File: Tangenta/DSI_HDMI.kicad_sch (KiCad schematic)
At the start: 40 parts, among them J8 HDMI_19PIN_043, U13 LT8912B

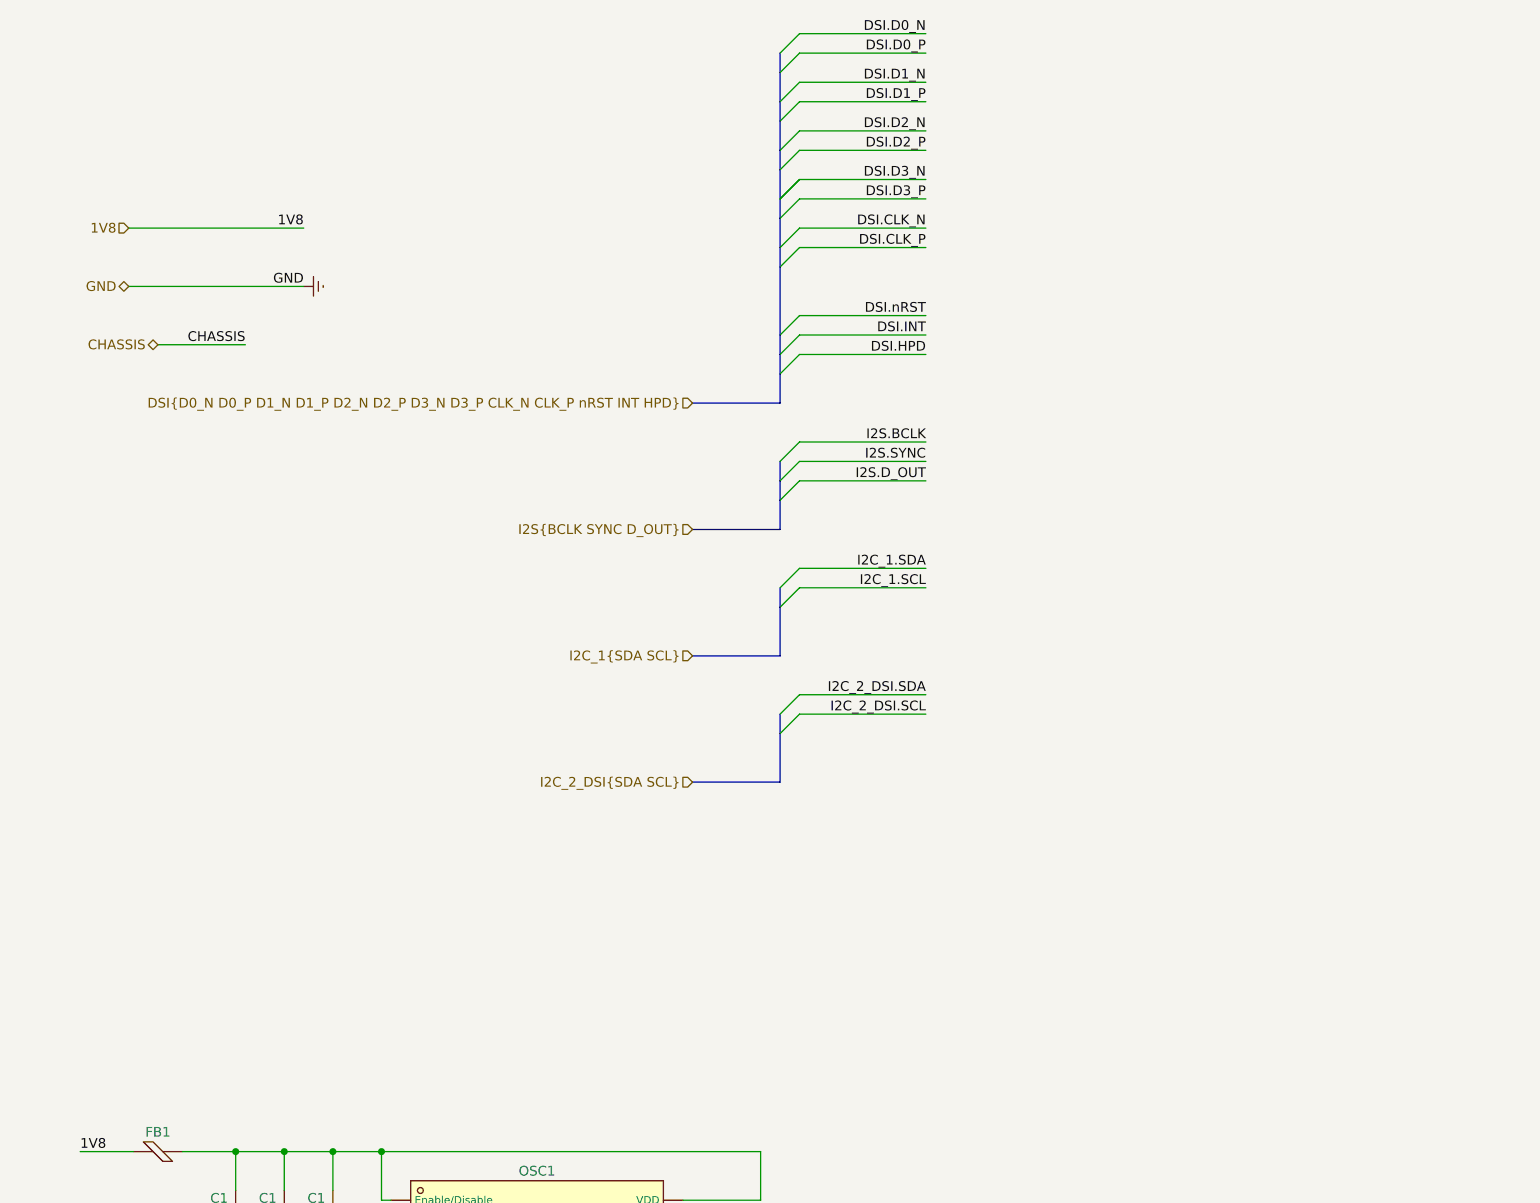
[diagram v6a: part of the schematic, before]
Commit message: HDMI port I2C with level shifter.
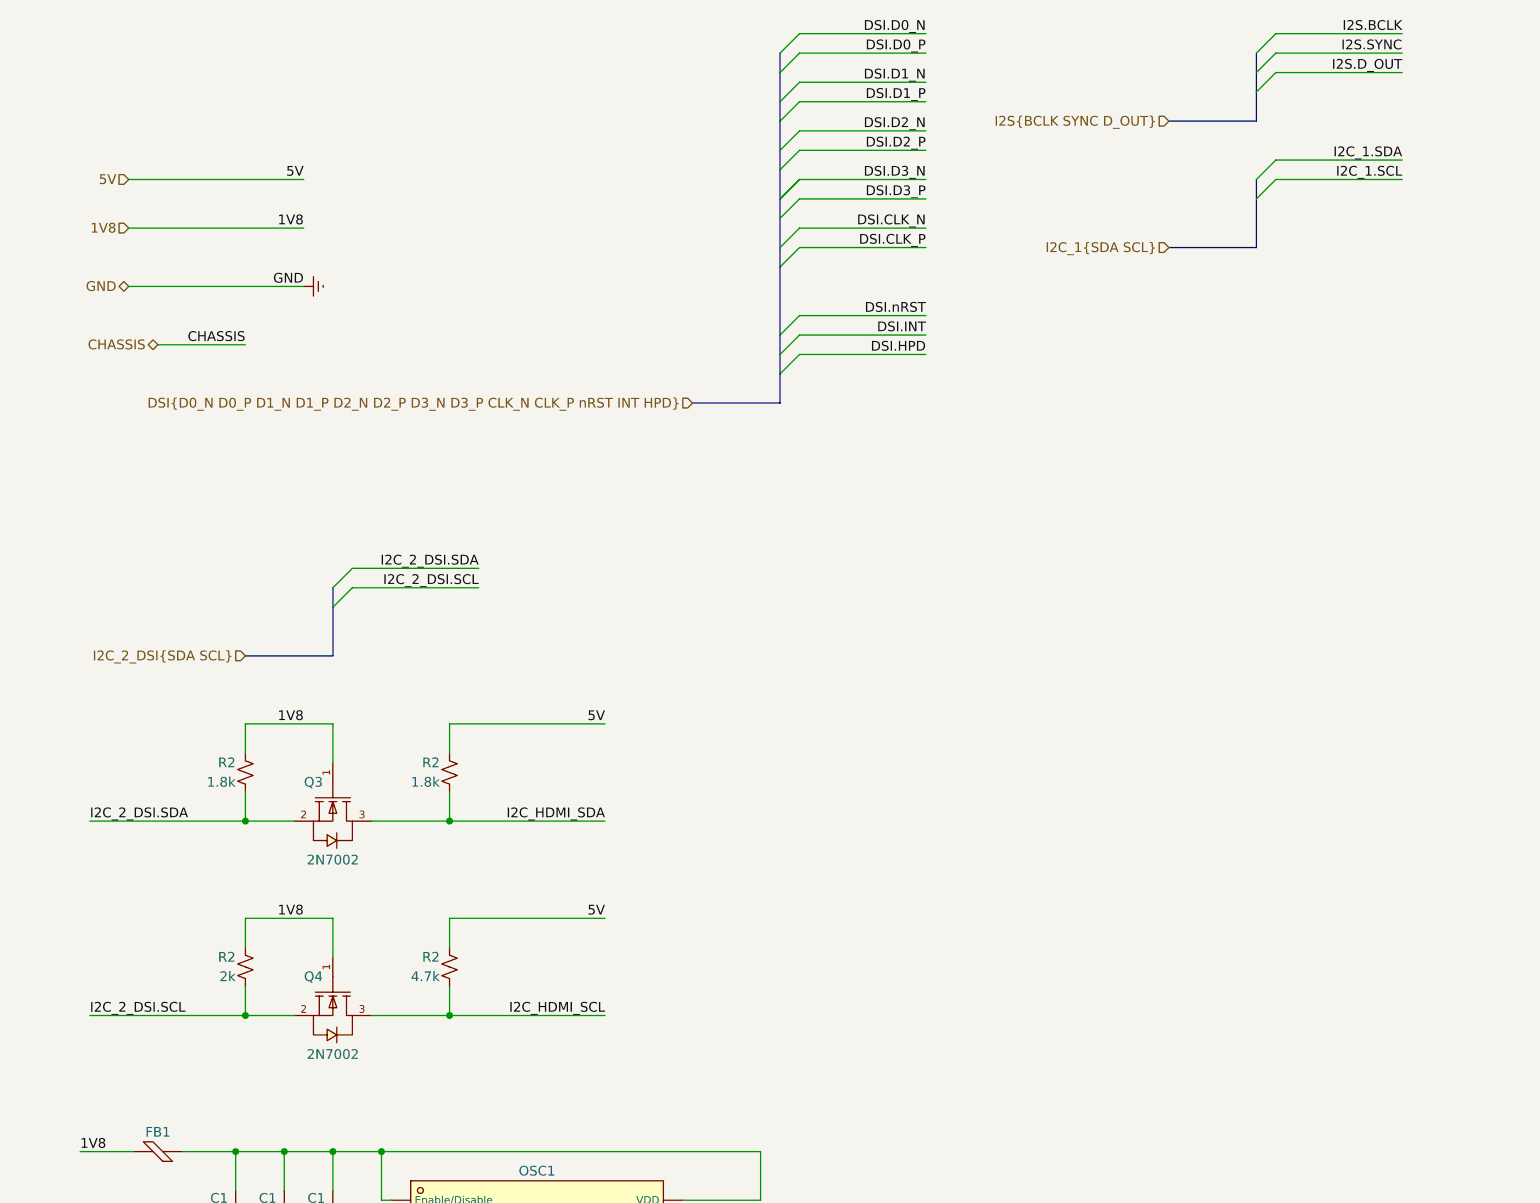
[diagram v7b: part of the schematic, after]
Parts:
- added Q3, Q4: 2N7002, NMOS_2N7002:NMOS_2N7002, symbol NMOS_2N7002:2N7002
- added R2: 4.7k, Resistor_SMD:R_0402_1005Metric, symbol Device:R_Small_US
- added R2: 2k, Resistor_SMD:R_0402_1005Metric, symbol Device:R_Small_US
- added R2 (x2): 1.8k, Resistor_SMD:R_0402_1005Metric, symbol Device:R_Small_US
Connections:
- net 1V8: now also Q3.1 (G), Q4.1 (G), R2.2, R2.2
- net I2C_2_DSI.SCL: now also Q4.2 (S), R2.1
- net I2C_2_DSI.SDA: now also Q3.2 (S), R2.1
- new net 5V: R2.2, R2.2
- new net I2C_HDMI_SCL: Q4.3 (D), R2.1
- new net I2C_HDMI_SDA: Q3.3 (D), R2.1

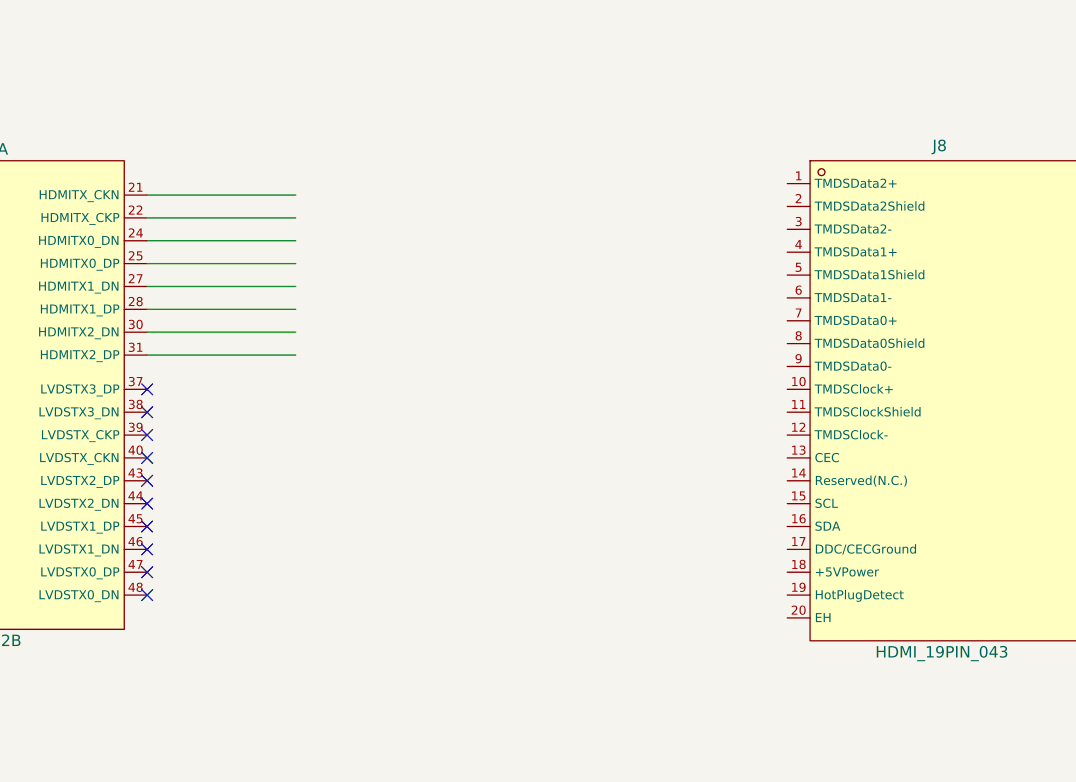
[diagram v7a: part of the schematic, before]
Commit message: Finished HDMI schematic...
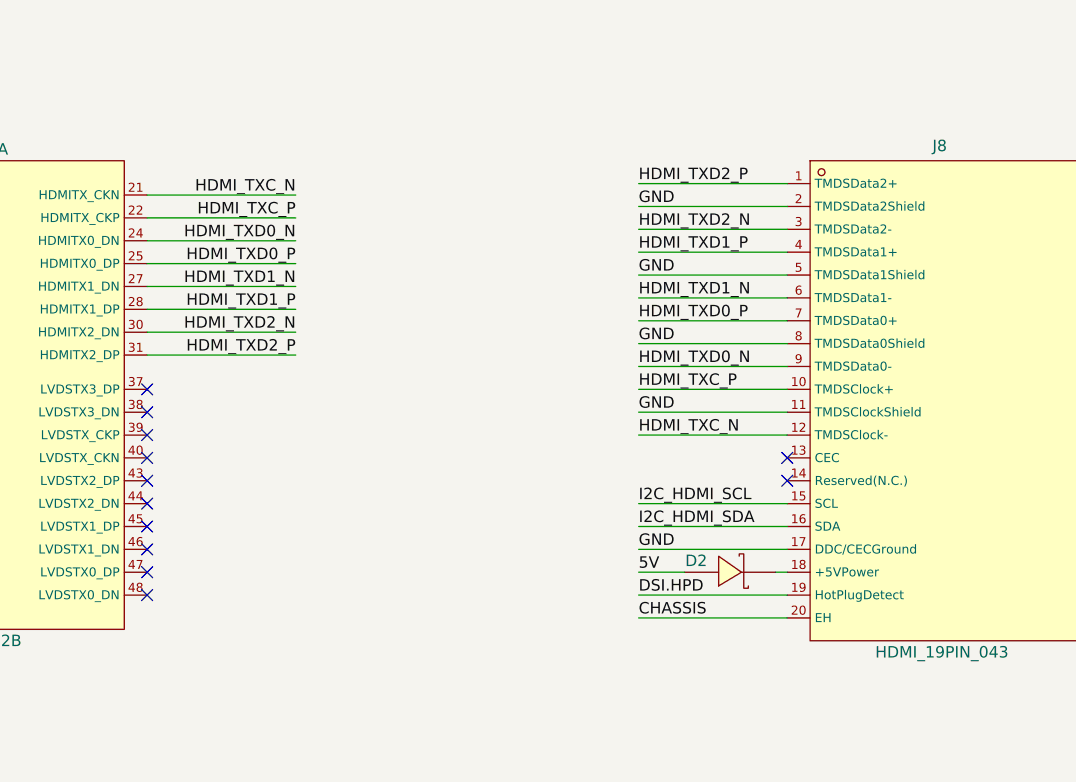
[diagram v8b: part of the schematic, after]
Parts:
- added D2: B540C-13-F, B540C-13-F:B540C-13-F, symbol B540C-13-F:B540C-13-F
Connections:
- net 5V: now also D2.2 (A)
- net CHASSIS: now also J8.20 (EH)
- net DSI.HPD: now also J8.19 (HotPlugDetect)
- net GNDREF: now also J8.11 (TMDSClockShield), J8.17 (DDC/CECGround), J8.2 (TMDSData2Shield), J8.5 (TMDSData1Shield), J8.8 (TMDSData0Shield)
- net I2C_HDMI_SCL: now also J8.15 (SCL)
- net I2C_HDMI_SDA: now also J8.16 (SDA)
- net HDMI_TXC_N: now reaches U13.21 (HDMITX_CKN)
- net HDMI_TXC_N: now also J8.12 (TMDSClock-)
- net HDMI_TXC_P: now reaches U13.22 (HDMITX_CKP)
- net HDMI_TXC_P: now also J8.10 (TMDSClock+)
- net HDMI_TXD0_N: now reaches U13.24 (HDMITX0_DN)
- net HDMI_TXD0_N: now also J8.9 (TMDSData0-)
- net HDMI_TXD0_P: now reaches U13.25 (HDMITX0_DP)
- net HDMI_TXD0_P: now also J8.7 (TMDSData0+)
- net HDMI_TXD1_N: now reaches U13.27 (HDMITX1_DN)
- net HDMI_TXD1_N: now also J8.6 (TMDSData1-)
- net HDMI_TXD1_P: now reaches U13.28 (HDMITX1_DP)
- net HDMI_TXD1_P: now also J8.4 (TMDSData1+)
- net HDMI_TXD2_N: now reaches U13.30 (HDMITX2_DN)
- net HDMI_TXD2_N: now also J8.3 (TMDSData2-)
- net HDMI_TXD2_P: now reaches U13.31 (HDMITX2_DP)
- net HDMI_TXD2_P: now also J8.1 (TMDSData2+)
- net at J8.18 (+5VPower): now also D2.1 (K)
- no-connect marks 15 -> 17
